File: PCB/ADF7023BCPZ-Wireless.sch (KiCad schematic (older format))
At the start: 0 parts

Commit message: Initial commit
Project created in KicAD< scheamtic near complete, components for sub
1GHZ RF system added to related libaries. Datasheets for components
added.
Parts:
- added BL?: 0868BM15C0001E, PCB_Footprints:0868BM15C0001E, symbol 0868BM15C0001E
- added C? (x2): CL05C180GB5NCNC, PCB_Footprints:C0402, symbol CL05C180GB5NCNC
- added C?: GRM155R71H152KA01D, PCB_Footprints:C0402, symbol GRM155R71H152KA01D
- added C? (x4): CL10B224JO8NNNC, PCB_Footprints:C0402, symbol CL10B224JO8NNNC
- added C? (x2): CL05B104JP5NNNC, PCB_Footprints:C0402, symbol CL05B104JP5NNNC
- added L?: 0402CS-12NXJL, PCB_Footprints:L0402, symbol 0402CS-12NXJL
- added L?: 0402CS-24NXJL, PCB_Footprints:L0402, symbol 0402CS-24NXJL
- added LED?: LTST-C193TBKT-5A, PCB_Footprints:LED0603, symbol LTST-C193TBKT-5A
- added R?: ERA-2AED363X, PCB_Footprints:R0603, symbol ERA-2AED363X
- added R?: RC1608J202CS, PCB_Footprints:R0603, symbol RC1608J202CS
- added T?: 1909763-1, PCB_Footprints:1909763-1, symbol 1909763-1
- added U?: ADF7023BCPZ, PCB_Footprints:ADF7023BCPZ, symbol ADF7023BCPZ
- added X?: FA-128_26.0000MF10Z-AC3, PCB_Footprints:FA-128_26.0000MF10Z-AC3, symbol FA-128_26.0000MF10Z-AC3
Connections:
- new net: C?.1, U?.13 (XOSC26P), X?.1
- new net: C?.1, U?.14 (XOSC26N), X?.3
- new net: C?.1, U?.12 (CWAKEUP)
- new net: C?.2, U?.1 (CREGRF1)
- new net: R?.2, U?.2 (RBIAS)
- new net: C?.2, U?.3 (CREGRF2)
- new net: C?.1, U?.15 (DGUARD), U?.16 (CREGDIG1)
- new net: C?.1, U?.10 (VCOGUARD), U?.9 (CREVGVCO)
- new net: R?.1, U?.17 (GPIO0)
- new net: LED?.1, R?.2
- new net: BL?.4 (BAL2), U?.4 (RFIO_1P)
- new net: BL?.3 (BAL1), U?.5 (RFIO_1N)
- new net: L?.1, L?.2
- new net +3V3: C?.1, C?.1, U?.29 (VDDBAT1), U?.7 (VDDBAT2)
- new net GND: BL?.2 (GND), BL?.5 (GND), BL?.6 (GND), C?.1, C?.1, C?.2, C?.2, C?.2, C?.2, C?.2, C?.2, C?.2, LED?.2, R?.1, T?.2, U?.33 (GND_EPAD), X?.2, X?.4
- new net RF_CS: U?.24 (CS)
- new net RF_IRQ: U?.20 (IRQ_GPIO3)
- new net RF_MISO: U?.21 (MISO)
- new net RF_MOSI: U?.23 (MOSI)
- new net RF_SCLK: U?.22 (SCLK)

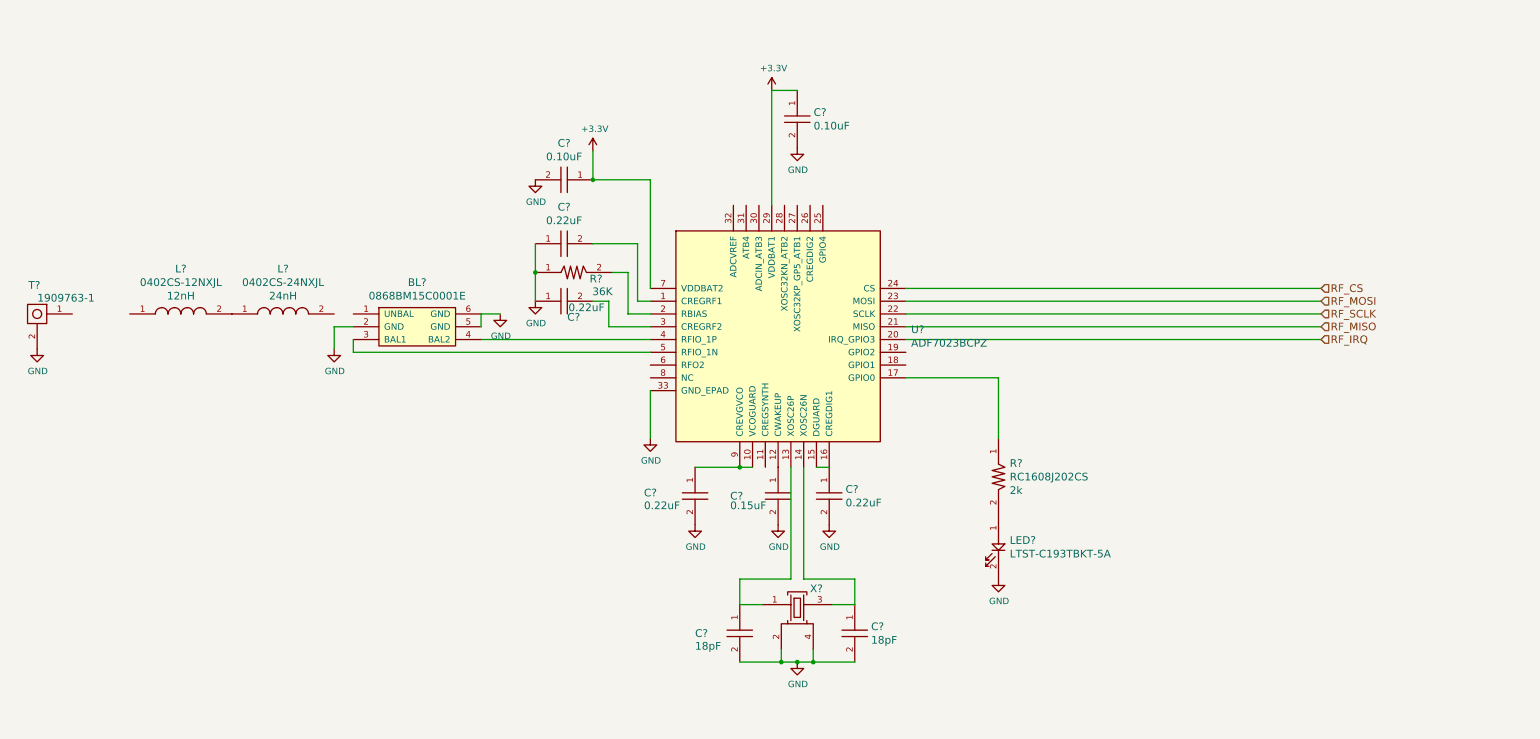
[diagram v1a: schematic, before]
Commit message: Sheets
Hiearchal sheet structure mostly established and linked. Need to
research more on OTA pgoramming with ADF7023 if possible.
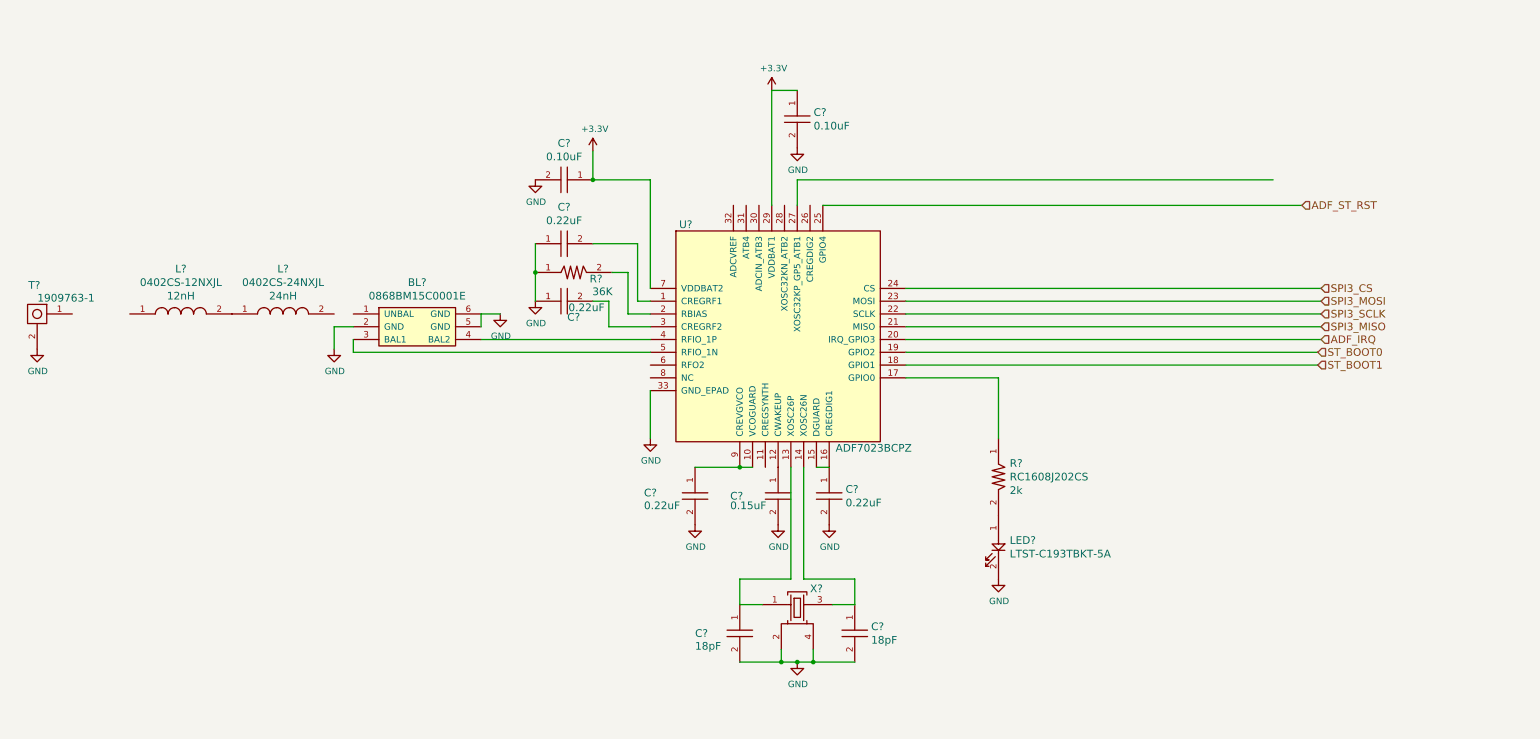
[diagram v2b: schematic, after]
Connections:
- net ST_BOOT1: now reaches U?.18 (GPIO1)
- net ST_BOOT0: now reaches U?.19 (GPIO2)
- net ADF_ST_RST: now reaches U?.25 (GPIO4)
- net RF_CS renamed SPI3_CS
- net RF_IRQ renamed ADF_IRQ
- net RF_MISO renamed SPI3_MISO
- net RF_MOSI renamed SPI3_MOSI
- net RF_SCLK renamed SPI3_SCLK
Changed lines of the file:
@@
 $EndComp
 Text HLabel 10725 2850 2    60   Input ~ 0
-RF_CS
+SPI3_CS
 Text HLabel 10725 2950 2    60   Input ~ 0
-RF_MOSI
+SPI3_MOSI
 Text HLabel 10725 3050 2    60   Input ~ 0
-RF_SCLK
+SPI3_SCLK
 Text HLabel 10725 3150 2    60   Input ~ 0
-RF_MISO
+SPI3_MISO
 Text HLabel 10725 3250 2    60   Input ~ 0
-RF_IRQ
+ADF_IRQ
 $Comp
 L RC1608J202CS R?
@@
 U 1 1 5817A575
 P 6525 3200
-F 0 "U?" H 7516 3228 60  0000 L CNN
-F 1 "ADF7023BCPZ" H 7516 3122 60  0000 L CNN
+F 0 "U?" H 5700 4050 60  0000 L CNN
+F 1 "ADF7023BCPZ" H 6925 2300 60  0000 L CNN
 F 2 "PCB_Footprints:ADF7023BCPZ" H 7675 6100 60  0001 C CNN
 F 3 "http://www.analog.com/media/en/technical-documentation/data-sheets/ADF7023.pdf" H 7725 4300 60  0001 C CNN
@@
 	6175 5125 6575 5125
 Wire Wire Line
-	6175 5775 7075 5775
+	6175 5775 6500 5775
+Wire Wire Line
+	6500 5775 6625 5775
+Wire Wire Line
+	6625 5775 6750 5775
+Wire Wire Line
+	6750 5775 7075 5775
 Wire Wire Line
 	6750 5675 6750 5775
@@
 	5025 2950 5150 2950
 Wire Wire Line
-	4575 2500 4575 2950
+	4575 2500 4575 2725
+Wire Wire Line
+	4575 2725 4575 2950
 Connection ~ 4575 2725
 Wire Wire Line
-	5825 4250 6275 4250
+	5825 4250 6175 4250
+Wire Wire Line
+	6175 4250 6275 4250
 Wire Wire Line
 	6775 4250 6875 4250
@@
 	1    0    0    -1
 $EndComp
+Text HLabel 10700 3350 2    60   Input ~ 0
+ST_BOOT0
+Text HLabel 10700 3450 2    60   Input ~ 0
+ST_BOOT1
+Text HLabel 10575 2200 2    60   Input ~ 0
+ADF_ST_RST
+Wire Wire Line
+	7475 3350 10700 3350
+Wire Wire Line
+	10700 3450 7475 3450
+Wire Wire Line
+	6625 2200 6625 2000
+Wire Wire Line
+	6625 2000 10350 2000
+Wire Wire Line
+	6825 2200 10575 2200
 $EndSCHEMATC

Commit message: RF
More progress on shaping out RF section schematic.
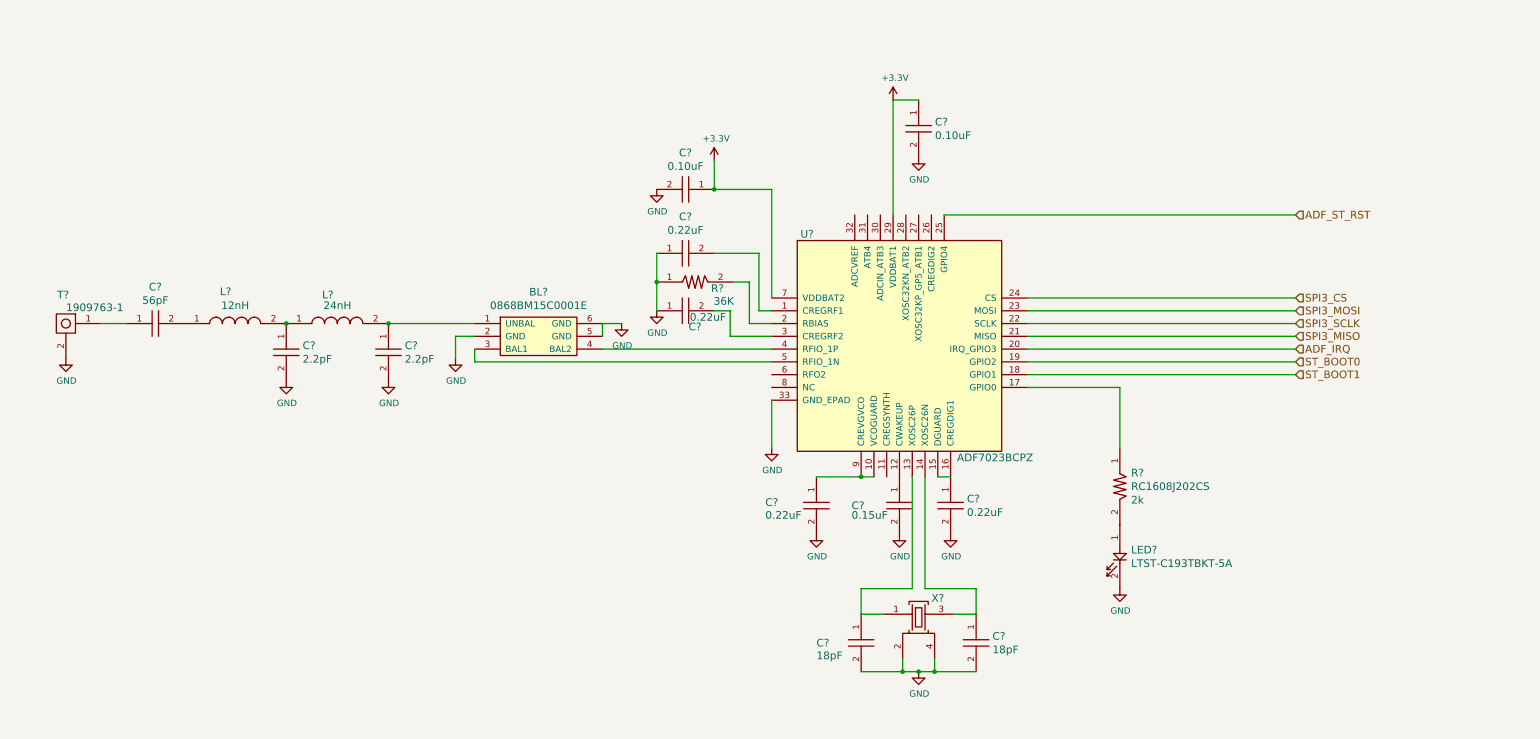
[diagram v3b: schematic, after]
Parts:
- added C? (x2): GRM1555C1H2R2CA01D, PCB_Footprints:C0402, symbol GRM1555C1H2R2CA01D
- added C?: CBR04C560F1GAC, PCB_Footprints:C0402, symbol CBR04C560F1GAC
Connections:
- net GND: now also C?.2, C?.2
- net at BL?.1 (UNBAL): now also L?.2, C?.1
- net at T?.1: now also C?.1
- net at L?.1: now also C?.2
- net at L?.1, L?.2: now also C?.1
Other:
- moved on the sheet: BL?, C?, L?, LED?, R?, T?, U?, X?

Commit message: Wireless Schematic Update
Wireless section schematic updated to be inline with S1G-RF
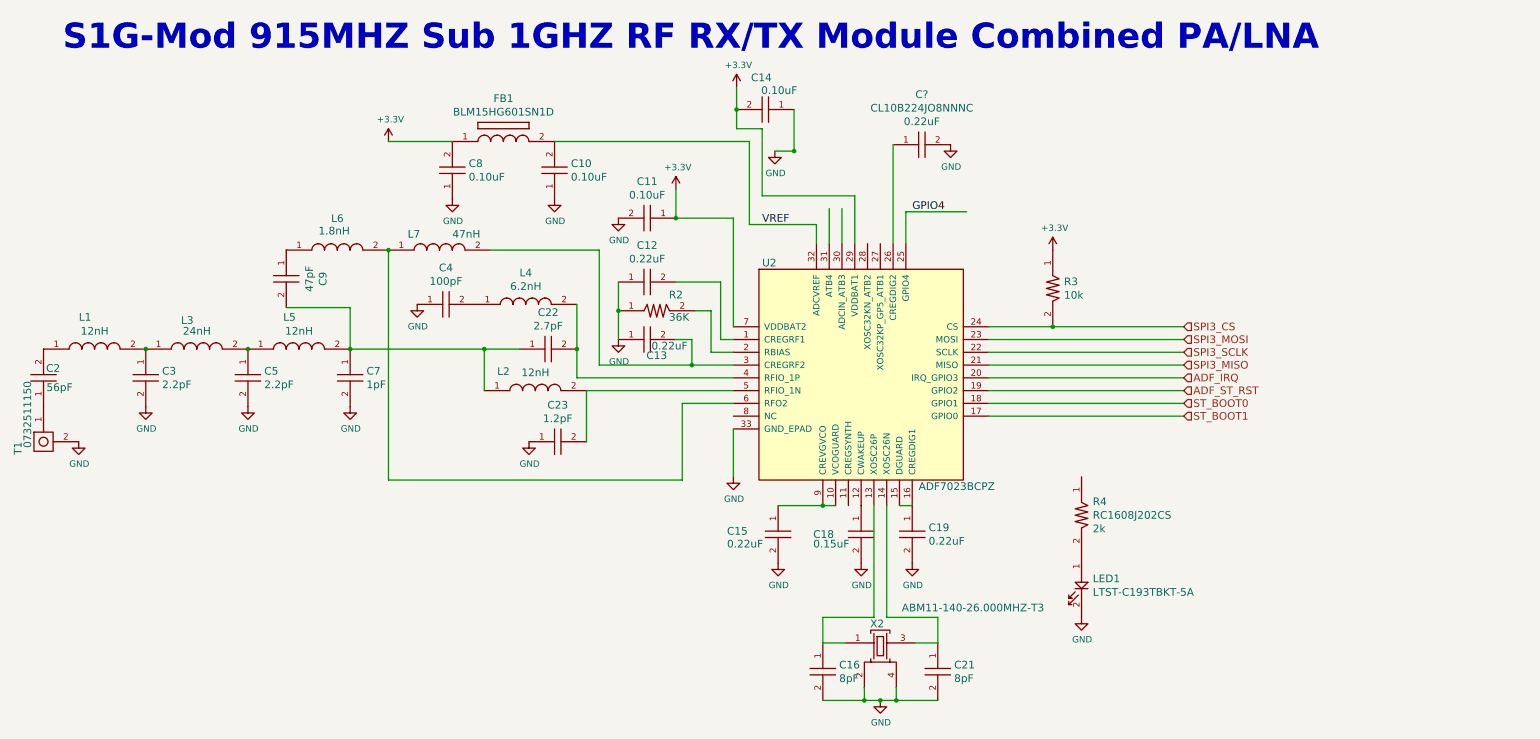
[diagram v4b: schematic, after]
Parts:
- removed BL?: 0868BM15C0001E, PCB_Footprints:0868BM15C0001E, symbol 0868BM15C0001E
- removed C? (x2): CL05C180GB5NCNC, PCB_Footprints:C0402, symbol CL05C180GB5NCNC
- removed C? (x2): GRM1555C1H2R2CA01D, PCB_Footprints:C0402, symbol GRM1555C1H2R2CA01D
- removed C?: CBR04C560F1GAC, PCB_Footprints:C0402, symbol CBR04C560F1GAC
- removed R?: ERA-2AED363X, PCB_Footprints:R0603, symbol ERA-2AED363X
- removed T?: 1909763-1, PCB_Footprints:1909763-1, symbol 1909763-1
- removed X?: FA-128_26.0000MF10Z-AC3, PCB_Footprints:FA-128_26.0000MF10Z-AC3, symbol FA-128_26.0000MF10Z-AC3
- added C10, C8: CL05B104JP5NNNC, PCB_Footprints:C0402, symbol CL05B104JP5NNNC
- added C16, C21: GRM0225C1E8R0WA03L, PCB_Footprints:C0402, symbol GRM0225C1E8R0WA03L
- added C2: CBR04C560F1GAC, PCB_Footprints:C0402, symbol CBR04C560F1GAC
- added C22: GRM1555C2A2R7CA01D, PCB_Footprints:C0402, symbol GRM1555C2A2R7CA01D
- added C23: GRM1555C1E1R2BA01D, PCB_Footprints:C0402, symbol GRM1555C1E1R2BA01D
- added C3, C5: GJM1555C1H2R2WB01D, PCB_Footprints:C0402, symbol GJM1555C1H2R2WB01D
- added C4: GRM1555C1H101GA01D, PCB_Footprints:C0402, symbol GRM1555C1H101GA01D
- added C7: GJM1555C1H1R0BB01D, PCB_Footprints:C0402, symbol GJM1555C1H1R0BB01D
- added C9: CBR04C470F3GAC, PCB_Footprints:C0402, symbol CBR04C470F3GAC
- added C?: CL10B224JO8NNNC, PCB_Footprints:C0402, symbol CL10B224JO8NNNC
- added FB1: BLM15HG601SN1D, PCB_Footprints:BLM15HG601SN1D, symbol BLM15HG601SN1D
- added L2, L5: 0402CS-12NXJL, PCB_Footprints:L0402, symbol 0402CS-12NXJL
- added L4: 0402CS-6N2XJL, PCB_Footprints:L0402, symbol 0402CS-6N2XJL
- added L6: 0402CS-1N8XJL, PCB_Footprints:L0402, symbol 0402CS-1N8XJL
- added L7: 0402CS-47NXJL, PCB_Footprints:L0402, symbol 0402CS-47NXJL
- added R2: ERA-2AEB363X, PCB_Footprints:R0402, symbol ERA-2AEB363X
- added R3: RC1005F103CS, PCB_Footprints:R0402, symbol RC1005F103CS
- added T1: 0732511150, PCB_Footprints:0732511150, symbol 0732511150
- added X2: ABM11-140-26.000MHZ-T3, PCB_Footprints:ABM11-140-26.000MHZ-T3, symbol ABM11-140-26.000MHZ-T3
- gave numbers to parts that had none: 12
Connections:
- net labels added: GPIO4, VREF
- wire segments 48 -> 66
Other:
- note added: "S1G-Mod 915MHZ Sub 1GHZ RF RX/TX Module Combined PA/LNA"
- moved on the sheet: C11, C12, C13, C14, C15, C18, C19, L1, L3, LED1, R4, U2
